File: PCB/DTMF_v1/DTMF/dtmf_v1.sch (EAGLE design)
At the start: 28 parts, among them IC1 ATTINY84A-SSF, IC2 MT8870DS1, Y1 ATS080B-E, Y2 ATS080B-E

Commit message: vault backup: 2023-12-27 10:32:53
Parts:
- removed L1, L2, L3, L4: (no value), adafruit:LEDCHIP-LED0805
- removed R4, R5, R6, R7: 330, rcl:R-US_M0805
- added L5: (no value), adafruit:LEDCHIP-LED0805
- added R11: 330, rcl:R-US_M0805
- added TP1, TP2, TP4, TP5, TP7: PTR1B1,27, testpad:PTR1B1,27
- added USER_IN_2: (no value), pinhead:PINHD-1X2
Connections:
- removed net N$17: L4.C, R7.1
- removed net N$20: L1.C, R4.1
- removed net N$6: IC1.PA1_(ADC1/AIN0/PCINT1), IC2.Q3, L2.A
- removed net N$8: IC1.PA3_(ADC3/T0/PCINT3), IC2.Q1, L4.A
- new net CUTDOWN: USER_IN_2.1
- new net N$25: L5.C, R11.1
- net GND: now also R11.2; no longer R4.2, R5.2, R6.2, R7.2
- net N$18: now also IC1.PA3_(ADC3/T0/PCINT3), IC2.Q1, TP5.TP; no longer L3.C, R6.1
- net N$19: now also IC1.PA1_(ADC1/AIN0/PCINT1), IC2.Q3, TP2.TP; no longer L2.C, R5.1
- net N$24: now also USER_IN_2.2
- net N$4: now also L5.A, TP7.TP
- net N$5: now also TP1.TP; no longer L1.A
- net N$7: now also TP4.TP; no longer L3.A

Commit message: modifications done on mac for the board
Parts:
- removed USER_IN_2: (no value), pinhead:PINHD-1X2
- added JP2: (no value), pinhead:PINHD-2X2
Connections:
- new net DROGUE: JP2.4
- net CUTDOWN: now also JP2.2; no longer USER_IN_2.1
- net N$22: now also JP2.3
- net N$24: now also JP2.1; no longer USER_IN_2.2
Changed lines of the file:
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@@
 <part name="GND7" library="supply1" library_urn="urn:adsk.eagle:library:371" deviceset="GND" device=""/>
 <part name="ICSP1" library="pinhead" library_urn="urn:adsk.eagle:library:325" deviceset="PINHD-2X3" device="" package3d_urn="urn:adsk.eagle:package:22462/2"/>
-<part name="USER_IN_2" library="pinhead" library_urn="urn:adsk.eagle:library:325" deviceset="PINHD-1X2" device="" package3d_urn="urn:adsk.eagle:package:22435/2"/>
 <part name="L5" library="adafruit" deviceset="LED" device="CHIP-LED0805"/>
 <part name="R11" library="rcl" library_urn="urn:adsk.eagle:library:334" deviceset="R-US_" device="M0805" package3d_urn="urn:adsk.eagle:package:23556/2" value="330"/>
@@
 <part name="TP5" library="testpad" library_urn="urn:adsk.eagle:library:385" deviceset="PTR1" device="B1,27" package3d_urn="urn:adsk.eagle:package:27944/2" value="PTR1B1,27"/>
 <part name="TP7" library="testpad" library_urn="urn:adsk.eagle:library:385" deviceset="PTR1" device="B1,27" package3d_urn="urn:adsk.eagle:package:27944/2" value="PTR1B1,27"/>
+<part name="JP2" library="pinhead" library_urn="urn:adsk.eagle:library:325" deviceset="PINHD-2X2" device="" package3d_urn="urn:adsk.eagle:package:22455/2"/>
 </parts>
 <sheets>
@@
 <attribute name="VALUE" x="-6.858" y="24.13" size="1.778" layer="96" rot="R90"/>
 </instance>
-<instance part="P+5" gate="VCC" x="55.88" y="25.4" smashed="yes">
-<attribute name="VALUE" x="53.34" y="22.86" size="1.778" layer="96" rot="R90"/>
+<instance part="P+5" gate="VCC" x="58.42" y="35.56" smashed="yes">
+<attribute name="VALUE" x="55.88" y="33.02" size="1.778" layer="96" rot="R90"/>
 </instance>
 <instance part="GND7" gate="1" x="55.88" y="5.08" smashed="yes">
@@
 <attribute name="VALUE" x="39.37" y="5.08" size="1.778" layer="96"/>
 </instance>
-<instance part="USER_IN_2" gate="G$1" x="134.62" y="25.4" smashed="yes" rot="R270">
-<attribute name="NAME" x="130.81" y="20.955" size="1.778" layer="95"/>
-<attribute name="VALUE" x="129.54" y="31.75" size="1.778" layer="96" rot="R270"/>
-</instance>
 <instance part="L5" gate="G$1" x="60.96" y="71.12" smashed="yes" rot="R90">
 <attribute name="NAME" x="65.532" y="74.676" size="1.778" layer="95" rot="R180"/>
@@
 <attribute name="NAME" x="67.31" y="77.724" size="1.778" layer="95" rot="R180"/>
 <attribute name="TP_SIGNAL_NAME" x="63.5" y="80.01" size="1.778" layer="97" rot="R90"/>
+</instance>
+<instance part="JP2" gate="A" x="137.16" y="17.78" smashed="yes">
+<attribute name="NAME" x="128.27" y="23.495" size="1.778" layer="95"/>
+<attribute name="VALUE" x="128.27" y="12.7" size="1.778" layer="96"/>
 </instance>
 </instances>
@@
 <label x="5.08" y="43.18" size="0.8128" layer="95" rot="R180" xref="yes"/>
 <wire x1="15.24" y1="43.18" x2="5.08" y2="43.18" width="0.1524" layer="91"/>
-<wire x1="15.24" y1="43.18" x2="15.24" y2="30.48" width="0.1524" layer="91"/>
-<wire x1="15.24" y1="30.48" x2="63.5" y2="30.48" width="0.1524" layer="91"/>
+<wire x1="15.24" y1="43.18" x2="15.24" y2="27.94" width="0.1524" layer="91"/>
+<wire x1="15.24" y1="27.94" x2="63.5" y2="27.94" width="0.1524" layer="91"/>
 <pinref part="ICSP1" gate="A" pin="4"/>
 <wire x1="50.8" y1="12.7" x2="63.5" y2="12.7" width="0.1524" layer="91"/>
-<wire x1="63.5" y1="12.7" x2="63.5" y2="30.48" width="0.1524" layer="91"/>
+<wire x1="63.5" y1="12.7" x2="63.5" y2="27.94" width="0.1524" layer="91"/>
 </segment>
 </net>
@@
 <segment>
 <pinref part="ICSP1" gate="A" pin="2"/>
-<wire x1="50.8" y1="15.24" x2="55.88" y2="15.24" width="0.1524" layer="91"/>
+<wire x1="50.8" y1="15.24" x2="58.42" y2="15.24" width="0.1524" layer="91"/>
 <pinref part="P+5" gate="VCC" pin="VCC"/>
-<wire x1="55.88" y1="15.24" x2="55.88" y2="22.86" width="0.1524" layer="91"/>
+<wire x1="58.42" y1="15.24" x2="58.42" y2="33.02" width="0.1524" layer="91"/>
 </segment>
 </net>
@@
 <net name="N$22" class="0">
 <segment>
-<pinref part="IC1" gate="G$1" pin="(PCINT7/ICP/OC0B/ADC7)_PA7"/>
 <pinref part="USER_INT" gate="G$1" pin="1"/>
-<wire x1="15.24" y1="45.72" x2="-10.16" y2="45.72" width="0.1524" layer="91"/>
 <wire x1="-10.16" y1="45.72" x2="-20.32" y2="45.72" width="0.1524" layer="91"/>
 <wire x1="-20.32" y1="45.72" x2="-20.32" y2="20.32" width="0.1524" layer="91"/>
 <pinref part="LED5" gate="G$1" pin="A"/>
 <wire x1="-10.16" y1="40.64" x2="-10.16" y2="45.72" width="0.1524" layer="91"/>
-<junction x="-10.16" y="45.72"/>
+<pinref part="IC1" gate="G$1" pin="(PCINT7/ICP/OC0B/ADC7)_PA7"/>
+<wire x1="15.24" y1="45.72" x2="-2.54" y2="45.72" width="0.1524" layer="91"/>
+<wire x1="-2.54" y1="45.72" x2="-10.16" y2="45.72" width="0.1524" layer="91"/>
+<wire x1="-2.54" y1="45.72" x2="-2.54" y2="30.48" width="0.1524" layer="91"/>
+<wire x1="-2.54" y1="30.48" x2="114.3" y2="30.48" width="0.1524" layer="91"/>
+<junction x="-2.54" y="45.72"/>
+<wire x1="114.3" y1="30.48" x2="114.3" y2="17.78" width="0.1524" layer="91"/>
+<pinref part="JP2" gate="A" pin="3"/>
+<wire x1="114.3" y1="17.78" x2="132.08" y2="17.78" width="0.1524" layer="91"/>
 </segment>
 </net>
@@
 <pinref part="IC1" gate="G$1" pin="PA5_(ADC5/DO/MISO/OC1B/PCINT5)"/>
 <wire x1="114.3" y1="43.18" x2="116.84" y2="43.18" width="0.1524" layer="91"/>
-<wire x1="116.84" y1="43.18" x2="116.84" y2="20.32" width="0.1524" layer="91"/>
-<wire x1="116.84" y1="20.32" x2="30.48" y2="20.32" width="0.1524" layer="91"/>
-<wire x1="30.48" y1="20.32" x2="30.48" y2="15.24" width="0.1524" layer="91"/>
+<wire x1="116.84" y1="43.18" x2="116.84" y2="22.86" width="0.1524" layer="91"/>
+<wire x1="116.84" y1="22.86" x2="35.56" y2="22.86" width="0.1524" layer="91"/>
+<wire x1="35.56" y1="22.86" x2="35.56" y2="15.24" width="0.1524" layer="91"/>
 <pinref part="ICSP1" gate="A" pin="1"/>
-<wire x1="30.48" y1="15.24" x2="43.18" y2="15.24" width="0.1524" layer="91"/>
-<wire x1="116.84" y1="20.32" x2="127" y2="20.32" width="0.1524" layer="91"/>
-<wire x1="127" y1="20.32" x2="127" y2="27.94" width="0.1524" layer="91"/>
-<junction x="116.84" y="20.32"/>
-<pinref part="USER_IN_2" gate="G$1" pin="2"/>
-<wire x1="127" y1="27.94" x2="134.62" y2="27.94" width="0.1524" layer="91"/>
+<wire x1="35.56" y1="15.24" x2="43.18" y2="15.24" width="0.1524" layer="91"/>
+<pinref part="JP2" gate="A" pin="1"/>
+<wire x1="132.08" y1="20.32" x2="116.84" y2="20.32" width="0.1524" layer="91"/>
+<wire x1="116.84" y1="20.32" x2="116.84" y2="22.86" width="0.1524" layer="91"/>
+<junction x="116.84" y="22.86"/>
 </segment>
 </net>
 <net name="CUTDOWN" class="0">
 <segment>
-<pinref part="USER_IN_2" gate="G$1" pin="1"/>
-<wire x1="137.16" y1="27.94" x2="152.4" y2="27.94" width="0.1524" layer="91"/>
-<label x="152.4" y="27.94" size="1.27" layer="95" xref="yes"/>
+<pinref part="JP2" gate="A" pin="2"/>
+<wire x1="142.24" y1="27.94" x2="152.4" y2="27.94" width="0.1524" layer="91"/>
+<wire x1="139.7" y1="20.32" x2="142.24" y2="20.32" width="0.1524" layer="91"/>
+<wire x1="142.24" y1="20.32" x2="142.24" y2="27.94" width="0.1524" layer="91"/>
+<label x="152.4" y="27.94" size="1.016" layer="95" xref="yes"/>
 </segment>
 </net>
@@
 </segment>
 </net>
+<net name="DROGUE" class="0">
+<segment>
+<pinref part="JP2" gate="A" pin="4"/>
+<wire x1="139.7" y1="17.78" x2="144.78" y2="17.78" width="0.1524" layer="91"/>
+<wire x1="144.78" y1="17.78" x2="144.78" y2="25.4" width="0.1524" layer="91"/>
+<wire x1="144.78" y1="25.4" x2="152.4" y2="25.4" width="0.1524" layer="91"/>
+<label x="152.4" y="25.4" size="1.016" layer="95" xref="yes"/>
+</segment>
+</net>

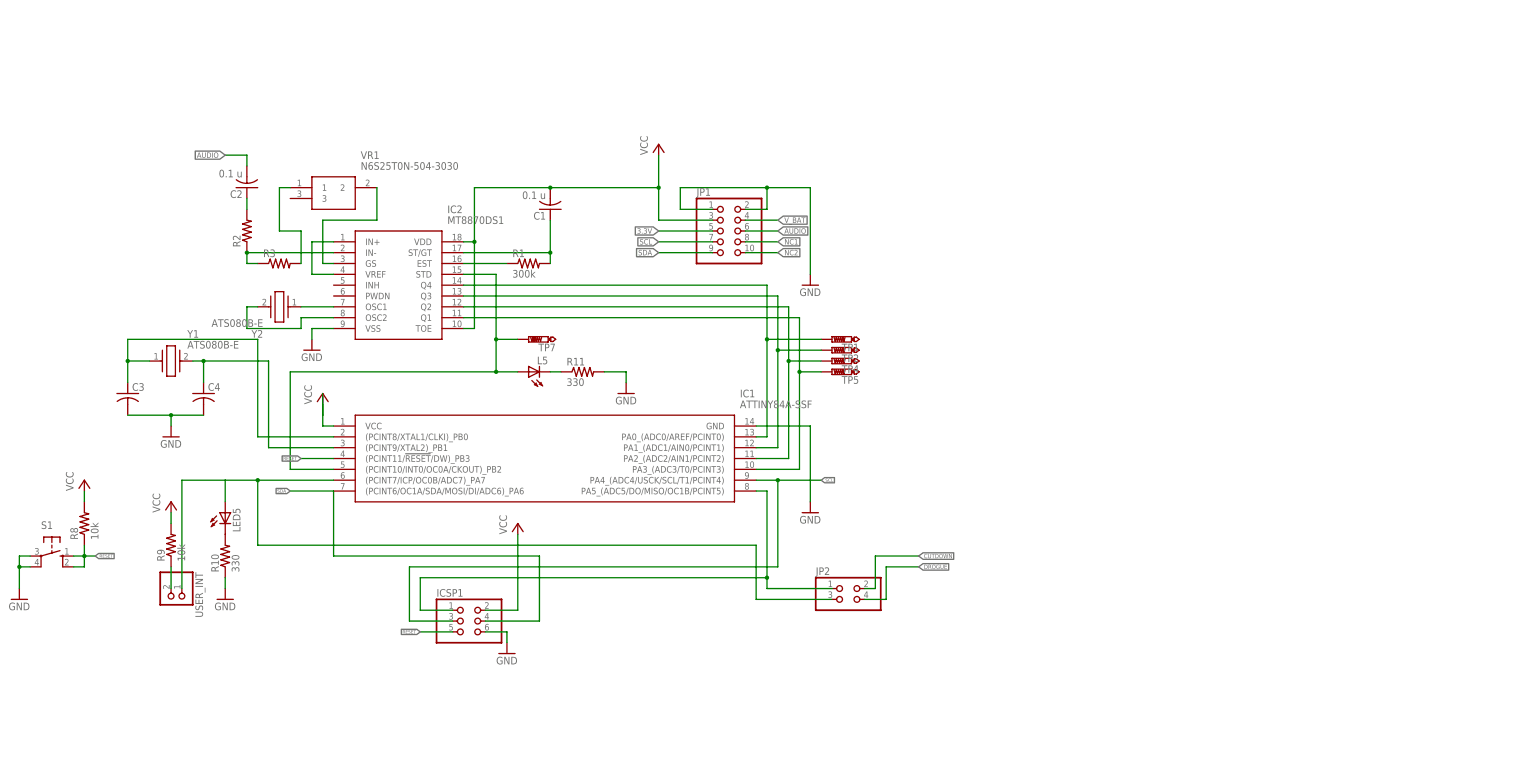
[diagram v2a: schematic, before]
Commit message: DTMF v1 completed with cutdown 30x100 mm form factor
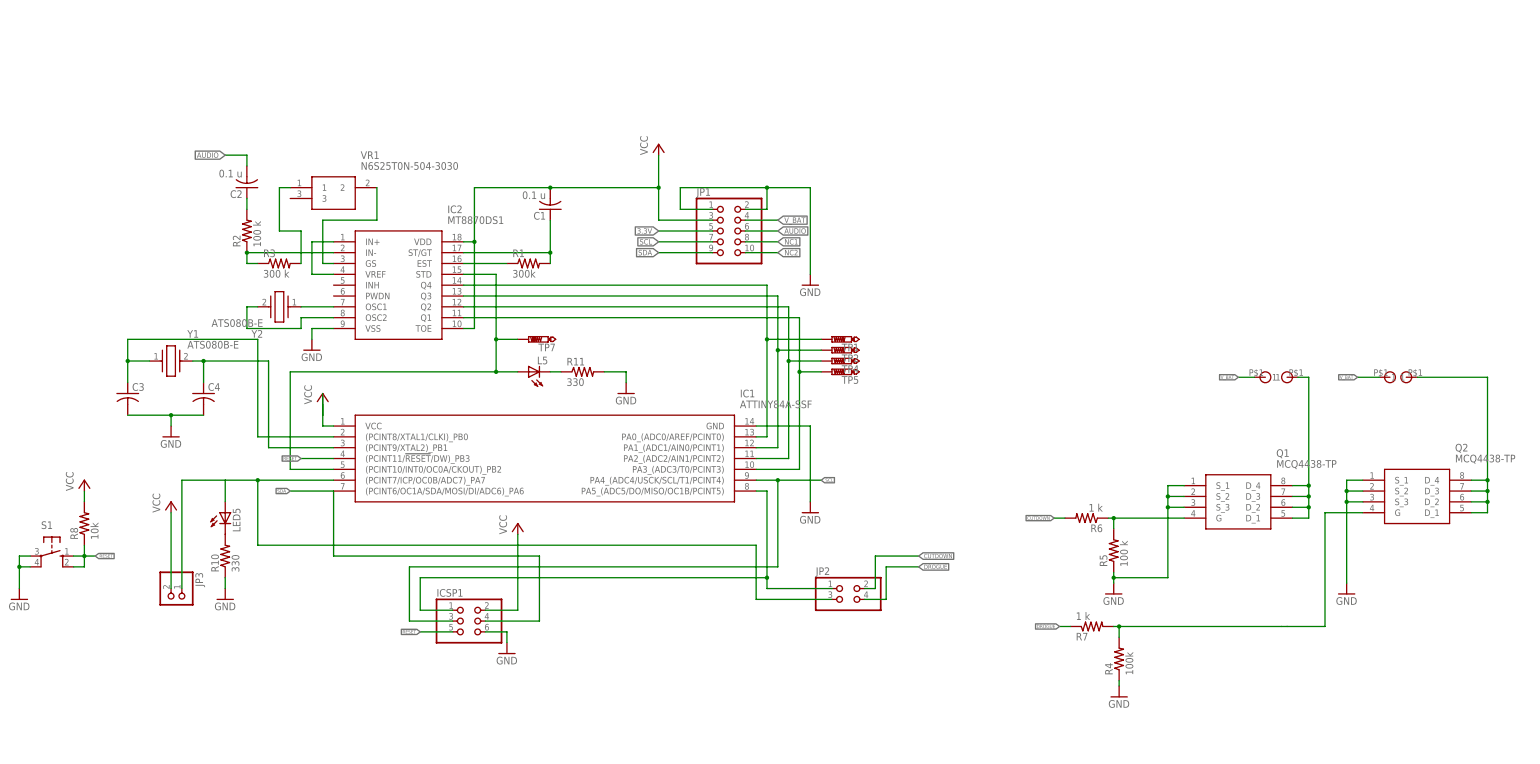
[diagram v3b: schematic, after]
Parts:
- removed R9: 10k, rcl:R-US_0207/10
- added Q1, Q2: MCQ4438-TP, MCQ4438-TP:MCQ4438-TP
- added R4: 100k, rcl:R-US_M0805
- added R5: 100 k, rcl:R-US_M0805
- added R6, R7: 1 k, rcl:R-US_M0805
- added U$1, U$2, U$3, U$4: M3_HOLE, KE8TJE:M3_HOLE
- R2: value (none) -> 100 k
- R3: value (none) -> 300 k
- renumbered USER_INT to JP3
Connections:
- removed net N$21: JP3.2, R9.1
- new net N$17: Q2.D_1, Q2.D_2, Q2.D_3, Q2.D_4, U$4.1
- new net N$20: Q1.D_1, Q1.D_2, Q1.D_3, Q1.D_4, U$2.1
- new net N$27: Q2.G, R4.2, R7.2
- new net N$6: Q1.G, R5.2, R6.1
- net CUTDOWN: now also R6.2
- net DROGUE: now also R7.1
- net GND: now also Q1.S_1, Q1.S_2, Q1.S_3, Q2.S_1, Q2.S_2, Q2.S_3, R4.1, R5.1
- net VCC: now also JP3.2; no longer R9.2
- net V_BAT: now also U$1.1, U$3.1

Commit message: cleaned the schematic for documentation
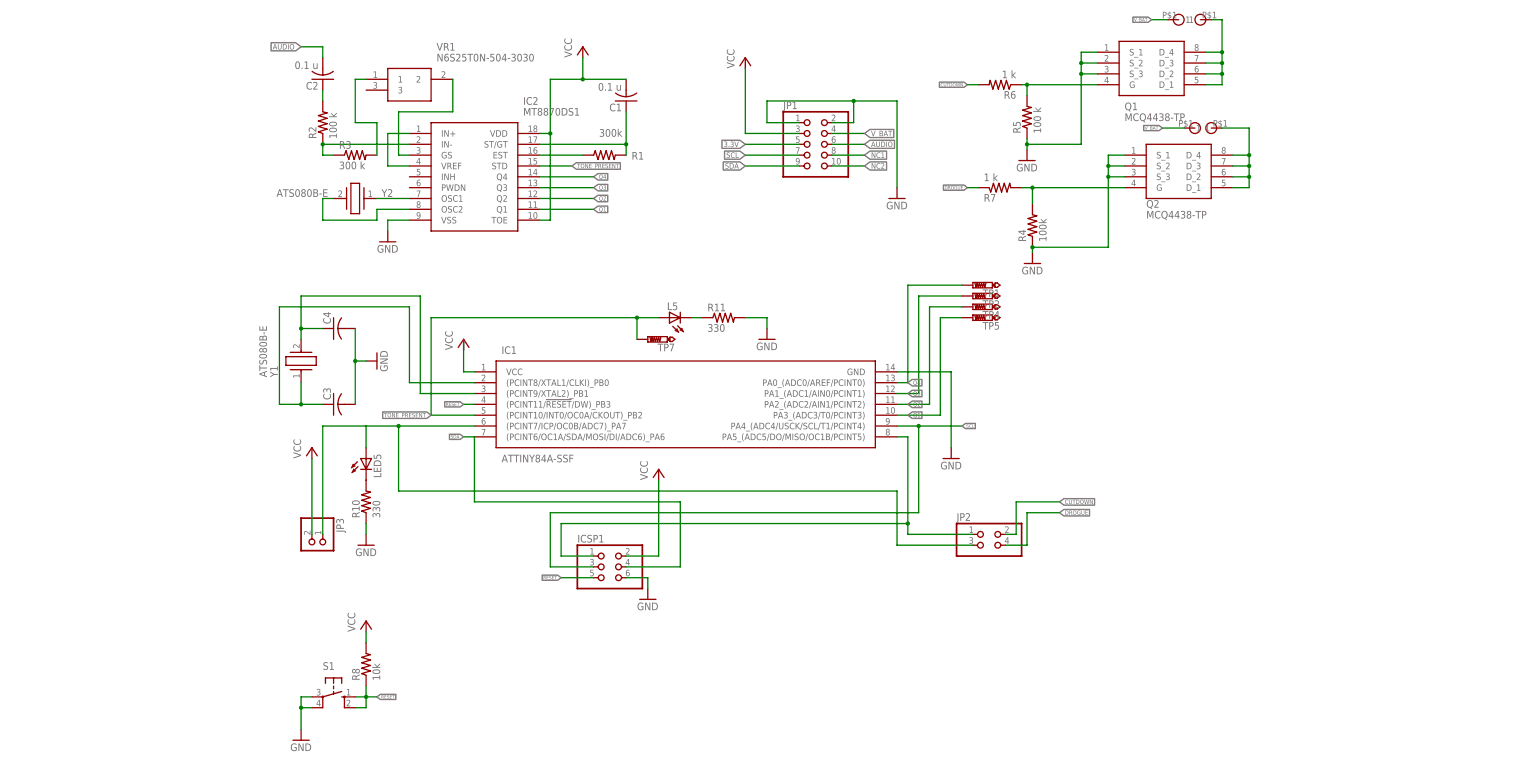
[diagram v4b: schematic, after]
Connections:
- net N$18 renamed Q1
- net N$19 renamed Q3
- net N$4 renamed TONE_PRESENT
- net N$5 renamed Q4
- net N$7 renamed Q2
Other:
- moved on the sheet: C1, C2, C3, C4, IC1, IC2, ICSP1, JP1, JP2, JP3, L5, LED5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

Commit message: modified PCB with JLC DRC file
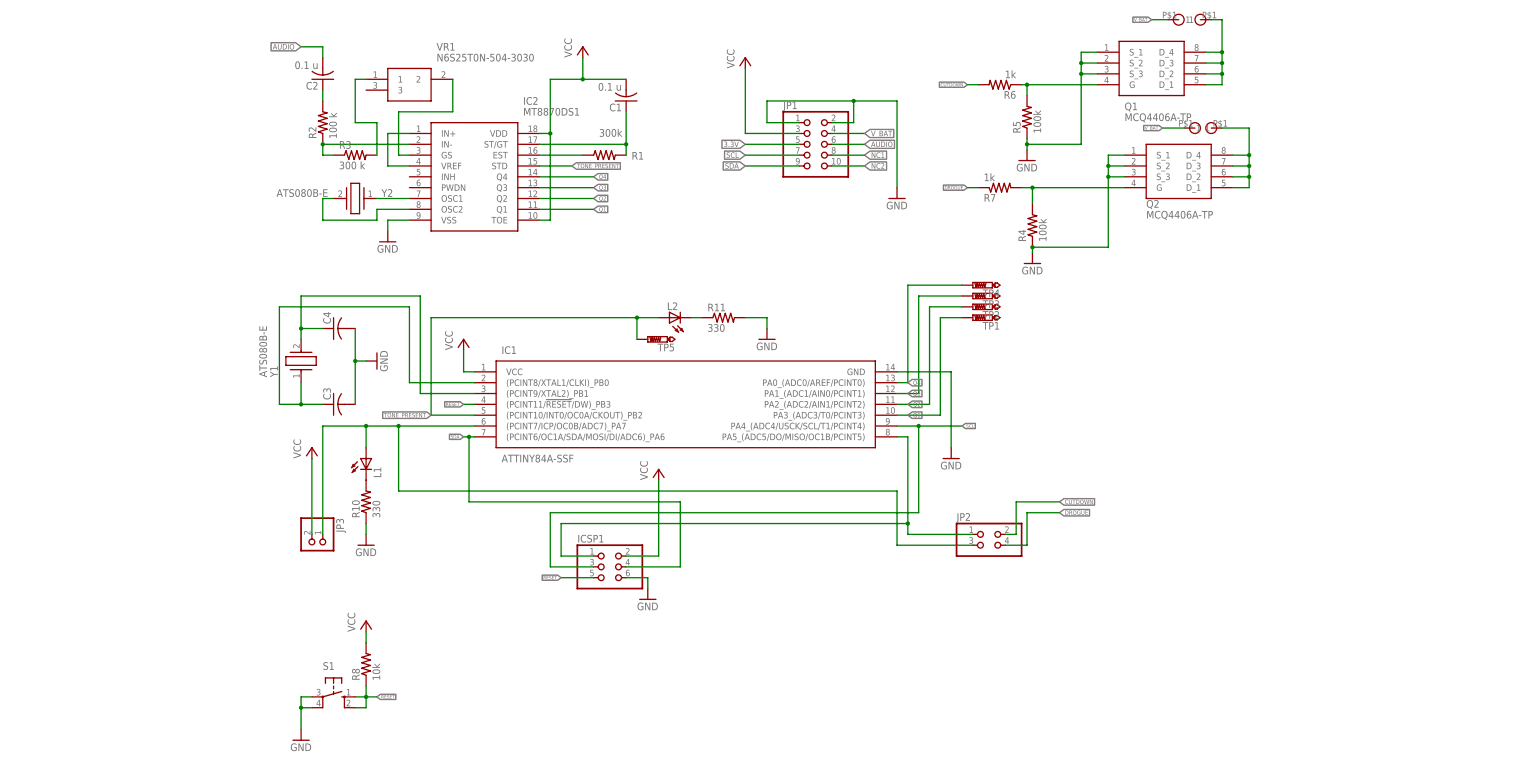
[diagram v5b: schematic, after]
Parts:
- removed TP7: PTR1B1,27, testpad:PTR1B1,27
- added TP3: PTR1B1,27, testpad:PTR1B1,27
- Q1, Q2: value MCQ4438-TP -> MCQ4406A-TP; device MCQ4438-TP:MCQ4438-TP -> MCQ4406A-TP:MCQ4406A-TP
- R5: value 100 k -> 100k
- R6, R7: value 1 k -> 1k
- renumbered L5 to L2, LED5 to L1
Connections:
- net Q1: now also TP1.TP; no longer TP5.TP
- net Q2: now also TP2.TP; no longer TP4.TP
- net Q3: now also TP3.TP; no longer TP2.TP
- net Q4: now also TP4.TP; no longer TP1.TP
- net TONE_PRESENT: now also TP5.TP; no longer TP7.TP
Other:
- moved on the sheet: TP1, TP2, TP4, TP5
